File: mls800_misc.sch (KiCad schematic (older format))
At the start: 18 parts, among them SW10 SW_TACT_LED_2, SW11 SW_TACT_LED_2, SW4 SW_TACT_LED_2, SW5 SW_TACT_LED_2, SW6 SW_TACT_LED_2, SW7 SW_TACT_LED_2, SW8 SW_TACT_LED_2, SW9 SW_TACT_LED_2, U4 MCP23017

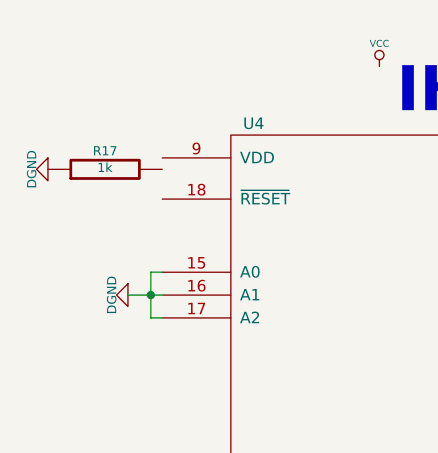
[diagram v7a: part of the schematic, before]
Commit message: MLS800 : created custom librairies
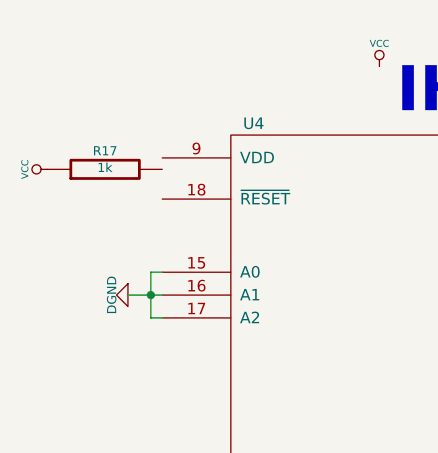
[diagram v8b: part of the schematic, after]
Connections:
- net DGND: no longer R17.1
- net VCC: now also R17.1
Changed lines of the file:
@@
 LIBS:contrib
 LIBS:valves
+LIBS:custom-i2c
+LIBS:custom-opto
+LIBS:custom-conn
+LIBS:custom-device
 LIBS:mls800-cache
 EELAYER 24 0
@@
 $Descr A4 11693 8268
 encoding utf-8
-Sheet 3 4
+Sheet 3 5
 Title ""
 Date "18 aug 2014"
@@
 $EndComp
 $Comp
-L DGND #PWR049
-U 1 1 53F19F7A
+L VCC #PWR?
+U 1 1 543C72E7
 P 750 1550
-F 0 "#PWR049" H 750 1550 40  0001 C CNN
-F 1 "DGND" H 750 1480 40  0000 C CNN
+F 0 "#PWR?" H 750 1650 30  0001 C CNN
+F 1 "VCC" H 750 1650 30  0000 C CNN
 F 2 "" H 750 1550 60  0000 C CNN
 F 3 "" H 750 1550 60  0000 C CNN
 	1    750  1550
-	0    1    1    0
+	0    -1   -1   0
 $EndComp
 $EndSCHEMATC
